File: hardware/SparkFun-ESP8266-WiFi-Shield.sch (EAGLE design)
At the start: 61 parts, among them Q1 BSS138, Q2 BSS138, U1 AP2112K-3.3V, U2 ESP8266, U3 AT25SF041-SOIC8, Y1 26MHz

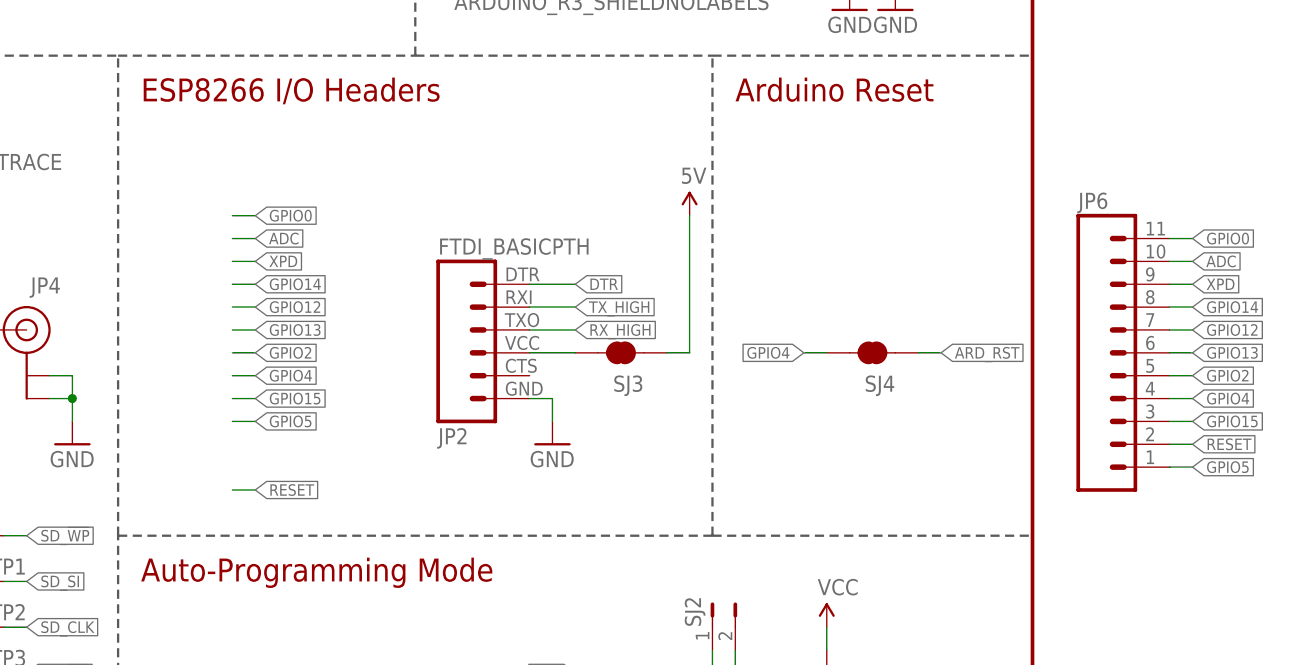
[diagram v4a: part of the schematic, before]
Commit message: Cleaning up schematic.
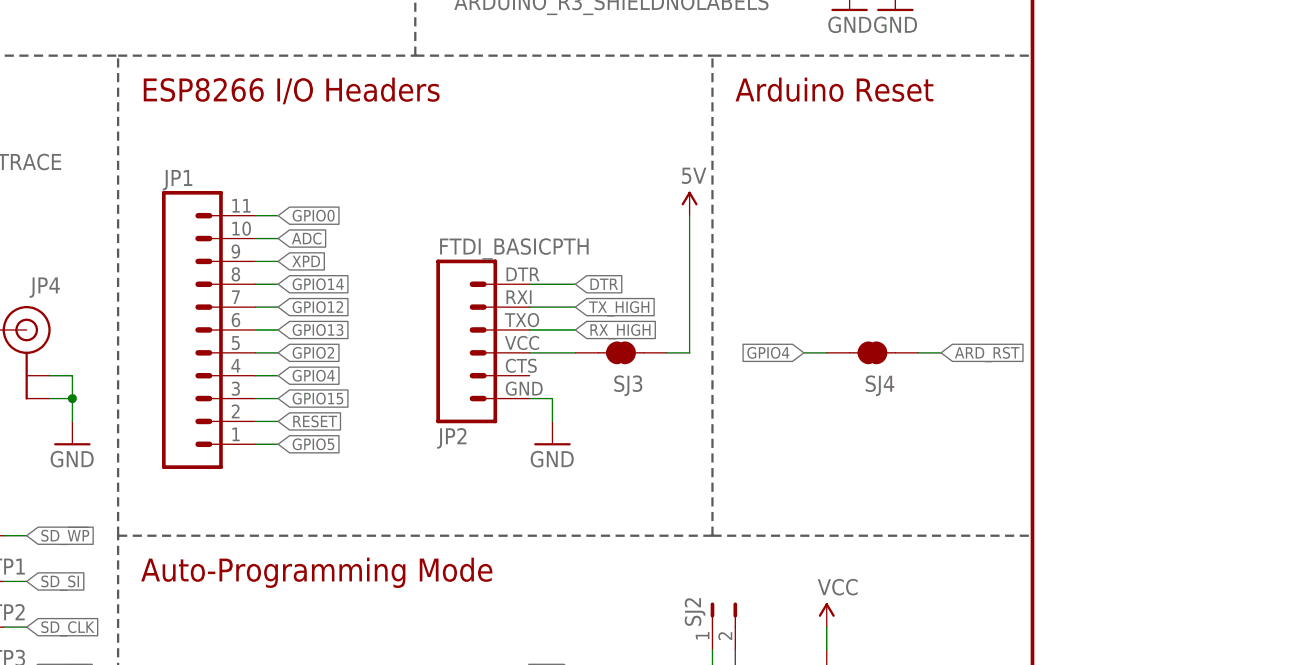
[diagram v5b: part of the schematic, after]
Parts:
- removed JP6: (no value), SparkFun-Connectors:M11PTH
- added JP1: (no value), SparkFun-Connectors:M11PTH
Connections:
- net ADC: now also JP1.10; no longer JP6.10
- net GPIO0: now also JP1.11; no longer JP6.11
- net GPIO12: now also JP1.7; no longer JP6.7
- net GPIO13: now also JP1.6; no longer JP6.6
- net GPIO14: now also JP1.8; no longer JP6.8
- net GPIO15: now also JP1.3; no longer JP6.3
- net GPIO2: now also JP1.5; no longer JP6.5
- net GPIO4: now also JP1.4; no longer JP6.4
- net GPIO5: now also JP1.1; no longer JP6.1
- net RESET: now also JP1.2; no longer JP6.2
- net XPD: now also JP1.9; no longer JP6.9
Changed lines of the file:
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@@
 <part name="SJ1" library="SparkFun-Passives" deviceset="JUMPER-PAD-2-NO" device="" value=""/>
 <part name="SJ2" library="SparkFun-Passives" deviceset="JUMPER-PTH-2-NO" device="" value=""/>
-<part name="JP6" library="SparkFun-Connectors" deviceset="M11" device="PTH"/>
+<part name="JP1" library="SparkFun-Connectors" deviceset="M11" device="PTH"/>
 </parts>
 <sheets>
@@
 <instance part="SJ1" gate="G$1" x="208.28" y="43.18"/>
 <instance part="SJ2" gate="G$1" x="213.36" y="58.42"/>
-<instance part="JP6" gate="G$1" x="254" y="88.9"/>
+<instance part="JP1" gate="G$1" x="152.4" y="91.44"/>
 </instances>
 <busses>
@@
 </segment>
 <segment>
-<wire x1="160.02" y1="73.66" x2="162.56" y2="73.66" width="0.1524" layer="91"/>
-<label x="162.56" y="73.66" size="1.27" layer="95" xref="yes"/>
-</segment>
-<segment>
-<pinref part="JP6" gate="G$1" pin="2"/>
-<wire x1="264.16" y1="78.74" x2="266.7" y2="78.74" width="0.1524" layer="91"/>
-<label x="266.7" y="78.74" size="1.27" layer="95" xref="yes"/>
+<pinref part="JP1" gate="G$1" pin="2"/>
+<wire x1="162.56" y1="81.28" x2="165.1" y2="81.28" width="0.1524" layer="91"/>
+<label x="165.1" y="81.28" size="1.27" layer="95" xref="yes"/>
 </segment>
 </net>
@@
 </segment>
 <segment>
-<wire x1="160.02" y1="96.52" x2="162.56" y2="96.52" width="0.1524" layer="91"/>
-<label x="162.56" y="96.52" size="1.27" layer="95" xref="yes"/>
-</segment>
-<segment>
-<pinref part="JP6" gate="G$1" pin="8"/>
-<wire x1="264.16" y1="93.98" x2="266.7" y2="93.98" width="0.1524" layer="91"/>
-<label x="266.7" y="93.98" size="1.27" layer="95" xref="yes"/>
+<pinref part="JP1" gate="G$1" pin="8"/>
+<wire x1="162.56" y1="96.52" x2="165.1" y2="96.52" width="0.1524" layer="91"/>
+<label x="165.1" y="96.52" size="1.27" layer="95" xref="yes"/>
 </segment>
 </net>
@@
 </segment>
 <segment>
-<wire x1="160.02" y1="101.6" x2="162.56" y2="101.6" width="0.1524" layer="91"/>
-<label x="162.56" y="101.6" size="1.27" layer="95" xref="yes"/>
-</segment>
-<segment>
-<pinref part="JP6" gate="G$1" pin="10"/>
-<wire x1="264.16" y1="99.06" x2="266.7" y2="99.06" width="0.1524" layer="91"/>
-<label x="266.7" y="99.06" size="1.27" layer="95" xref="yes"/>
+<pinref part="JP1" gate="G$1" pin="10"/>
+<wire x1="162.56" y1="101.6" x2="165.1" y2="101.6" width="0.1524" layer="91"/>
+<label x="165.1" y="101.6" size="1.27" layer="95" xref="yes"/>
 </segment>
 </net>
@@
 </segment>
 <segment>
-<wire x1="160.02" y1="104.14" x2="162.56" y2="104.14" width="0.1524" layer="91"/>
-<label x="162.56" y="104.14" size="1.27" layer="95" xref="yes"/>
-</segment>
-<segment>
-<pinref part="JP6" gate="G$1" pin="11"/>
-<wire x1="264.16" y1="101.6" x2="266.7" y2="101.6" width="0.1524" layer="91"/>
-<label x="266.7" y="101.6" size="1.27" layer="95" xref="yes"/>
+<pinref part="JP1" gate="G$1" pin="11"/>
+<wire x1="162.56" y1="104.14" x2="165.1" y2="104.14" width="0.1524" layer="91"/>
+<label x="165.1" y="104.14" size="1.27" layer="95" xref="yes"/>
 </segment>
 </net>
@@
 </segment>
 <segment>
-<wire x1="160.02" y1="81.28" x2="162.56" y2="81.28" width="0.1524" layer="91"/>
-<label x="162.56" y="81.28" size="1.27" layer="95" xref="yes"/>
-</segment>
-<segment>
-<pinref part="JP6" gate="G$1" pin="1"/>
-<wire x1="264.16" y1="76.2" x2="266.7" y2="76.2" width="0.1524" layer="91"/>
-<label x="266.7" y="76.2" size="1.27" layer="95" xref="yes"/>
+<pinref part="JP1" gate="G$1" pin="1"/>
+<wire x1="162.56" y1="78.74" x2="165.1" y2="78.74" width="0.1524" layer="91"/>
+<label x="165.1" y="78.74" size="1.27" layer="95" xref="yes"/>
 </segment>
 </net>
@@
 </segment>
 <segment>
-<wire x1="160.02" y1="86.36" x2="162.56" y2="86.36" width="0.1524" layer="91"/>
-<label x="162.56" y="86.36" size="1.27" layer="95" xref="yes"/>
-</segment>
-<segment>
 <pinref part="SJ4" gate="G$1" pin="2"/>
 <wire x1="226.06" y1="88.9" x2="223.52" y2="88.9" width="0.1524" layer="91"/>
@@
 </segment>
 <segment>
-<pinref part="JP6" gate="G$1" pin="4"/>
-<wire x1="264.16" y1="83.82" x2="266.7" y2="83.82" width="0.1524" layer="91"/>
-<label x="266.7" y="83.82" size="1.27" layer="95" xref="yes"/>
+<pinref part="JP1" gate="G$1" pin="4"/>
+<wire x1="162.56" y1="86.36" x2="165.1" y2="86.36" width="0.1524" layer="91"/>
+<label x="165.1" y="86.36" size="1.27" layer="95" xref="yes"/>
 </segment>
 </net>
@@
 </segment>
 <segment>
-<wire x1="160.02" y1="99.06" x2="162.56" y2="99.06" width="0.1524" layer="91"/>
-<label x="162.56" y="99.06" size="1.27" layer="95" xref="yes"/>
-</segment>
-<segment>
-<pinref part="JP6" gate="G$1" pin="9"/>
-<wire x1="264.16" y1="96.52" x2="266.7" y2="96.52" width="0.1524" layer="91"/>
-<label x="266.7" y="96.52" size="1.27" layer="95" xref="yes"/>
+<pinref part="JP1" gate="G$1" pin="9"/>
+<wire x1="162.56" y1="99.06" x2="165.1" y2="99.06" width="0.1524" layer="91"/>
+<label x="165.1" y="99.06" size="1.27" layer="95" xref="yes"/>
 </segment>
 </net>
@@
 </segment>
 <segment>
-<wire x1="160.02" y1="83.82" x2="162.56" y2="83.82" width="0.1524" layer="91"/>
-<label x="162.56" y="83.82" size="1.27" layer="95" xref="yes"/>
-</segment>
-<segment>
-<pinref part="JP6" gate="G$1" pin="3"/>
-<wire x1="264.16" y1="81.28" x2="266.7" y2="81.28" width="0.1524" layer="91"/>
-<label x="266.7" y="81.28" size="1.27" layer="95" xref="yes"/>
+<pinref part="JP1" gate="G$1" pin="3"/>
+<wire x1="162.56" y1="83.82" x2="165.1" y2="83.82" width="0.1524" layer="91"/>
+<label x="165.1" y="83.82" size="1.27" layer="95" xref="yes"/>
 </segment>
 </net>
@@
 </segment>
 <segment>
-<wire x1="160.02" y1="91.44" x2="162.56" y2="91.44" width="0.1524" layer="91"/>
-<label x="162.56" y="91.44" size="1.27" layer="95" xref="yes"/>
-</segment>
-<segment>
-<pinref part="JP6" gate="G$1" pin="6"/>
-<wire x1="264.16" y1="88.9" x2="266.7" y2="88.9" width="0.1524" layer="91"/>
-<label x="266.7" y="88.9" size="1.27" layer="95" xref="yes"/>
+<pinref part="JP1" gate="G$1" pin="6"/>
+<wire x1="162.56" y1="91.44" x2="165.1" y2="91.44" width="0.1524" layer="91"/>
+<label x="165.1" y="91.44" size="1.27" layer="95" xref="yes"/>
 </segment>
 </net>
@@
 </segment>
 <segment>
-<wire x1="160.02" y1="93.98" x2="162.56" y2="93.98" width="0.1524" layer="91"/>
-<label x="162.56" y="93.98" size="1.27" layer="95" xref="yes"/>
-</segment>
-<segment>
-<pinref part="JP6" gate="G$1" pin="7"/>
-<wire x1="264.16" y1="91.44" x2="266.7" y2="91.44" width="0.1524" layer="91"/>
-<label x="266.7" y="91.44" size="1.27" layer="95" xref="yes"/>
+<pinref part="JP1" gate="G$1" pin="7"/>
+<wire x1="162.56" y1="93.98" x2="165.1" y2="93.98" width="0.1524" layer="91"/>
+<label x="165.1" y="93.98" size="1.27" layer="95" xref="yes"/>
 </segment>
 </net>
@@
 </segment>
 <segment>
-<wire x1="160.02" y1="88.9" x2="162.56" y2="88.9" width="0.1524" layer="91"/>
-<label x="162.56" y="88.9" size="1.27" layer="95" xref="yes"/>
-</segment>
-<segment>
-<pinref part="JP6" gate="G$1" pin="5"/>
-<wire x1="264.16" y1="86.36" x2="266.7" y2="86.36" width="0.1524" layer="91"/>
-<label x="266.7" y="86.36" size="1.27" layer="95" xref="yes"/>
-</segment>
-</net>
+<pinref part="JP1" gate="G$1" pin="5"/>
+<wire x1="162.56" y1="88.9" x2="165.1" y2="88.9" width="0.1524" layer="91"/>
+<label x="165.1" y="88.9" size="1.27" layer="95" xref="yes"/>
+</segment>
+</net>

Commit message: Minor mods after running checklist.
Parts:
- SJ4: value JUMPER-PAD-2-NC_BY_TRACE -> JUMPER-PAD-2-NOYES_SILK; device SparkFun-Passives:JUMPER-PAD-2-NC_BY_TRACE -> SparkFun-Passives:JUMPER-PAD-2-NOYES_SILK
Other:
- note added: "SJ3 allows powering the ESP8266 from an FTDI cable. (Default: closed)."
- note added: "SJ4 connects the ESP8266 GPIO4 pin to the Arduino reset pin. With the proper ESP8266 firmware, this enables wireless Arduino bootloading. (Default: open)"
- moved on the sheet: JP2, SJ3
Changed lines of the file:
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@@
 <drawing>
 <settings>
-<setting alwaysvectorfont="no"/>
+<setting alwaysvectorfont="yes"/>
 <setting verticaltext="up"/>
 </settings>
@@
 <part name="JP4" library="SparkFun-Connectors" deviceset="U.FL" device="" value="U.FL"/>
 <part name="SUPPLY15" library="SparkFun-Aesthetics" deviceset="VCC" device=""/>
-<part name="SJ4" library="SparkFun-Passives" deviceset="JUMPER-PAD-2-NC_BY_TRACE" device="" value=""/>
 <part name="SJ1" library="SparkFun-Passives" deviceset="JUMPER-PAD-2-NO" device="" value=""/>
 <part name="SJ2" library="SparkFun-Passives" deviceset="JUMPER-PTH-2-NO" device="" value=""/>
 <part name="JP1" library="SparkFun-Connectors" deviceset="M11" device="PTH"/>
+<part name="SJ4" library="SparkFun-Passives" deviceset="JUMPER-PAD-2-NO" device="YES_SILK" value=""/>
 </parts>
 <sheets>
@@
 <wire x1="213.36" y1="68.58" x2="213.36" y2="121.92" width="0.254" layer="97" style="longdash"/>
 <text x="215.9" y="116.84" size="2.54" layer="94">Arduino Reset</text>
+<text x="215.9" y="96.52" size="1.27" layer="97">SJ4 connects the ESP8266
+GPIO4 pin to the Arduino
+reset pin. With the proper
+ESP8266 firmware, this
+enables wireless Arduino
+bootloading.
+(Default: open)</text>
+<text x="190.5" y="76.2" size="1.27" layer="97">SJ3 allows powering
+the ESP8266 from
+an FTDI cable.
+(Default: closed).</text>
 </plain>
 <instances>
@@
 <instance part="SUPPLY11" gate="G$1" x="157.48" y="172.72"/>
 <instance part="SUPPLY7" gate="G$1" x="116.84" y="175.26"/>
-<instance part="JP2" gate="G$1" x="187.96" y="91.44" rot="MR180"/>
-<instance part="GND17" gate="1" x="195.58" y="78.74"/>
-<instance part="SUPPLY12" gate="G$1" x="210.82" y="104.14"/>
+<instance part="JP2" gate="G$1" x="180.34" y="91.44" rot="MR180"/>
+<instance part="GND17" gate="1" x="187.96" y="78.74"/>
+<instance part="SUPPLY12" gate="G$1" x="203.2" y="104.14"/>
 <instance part="LOGO1" gate="G$1" x="0" y="0"/>
 <instance part="STANDOFF1" gate="G$1" x="243.84" y="33.02"/>
@@
 <instance part="S1" gate="G$1" x="127" y="137.16"/>
 <instance part="D2" gate="G$1" x="99.06" y="53.34" rot="R270"/>
-<instance part="SJ3" gate="G$1" x="203.2" y="88.9" rot="R180"/>
+<instance part="SJ3" gate="G$1" x="195.58" y="88.9" rot="R180"/>
 <instance part="JP4" gate="G$1" x="137.16" y="91.44" rot="MR0"/>
 <instance part="SUPPLY15" gate="G$1" x="104.14" y="55.88"/>
-<instance part="SJ4" gate="G$1" x="231.14" y="88.9" rot="R180"/>
 <instance part="SJ1" gate="G$1" x="208.28" y="43.18"/>
 <instance part="SJ2" gate="G$1" x="213.36" y="58.42"/>
 <instance part="JP1" gate="G$1" x="152.4" y="91.44"/>
+<instance part="SJ4" gate="G$1" x="231.14" y="88.9" rot="R180"/>
 </instances>
 <busses>
@@
 <segment>
 <pinref part="JP2" gate="G$1" pin="6"/>
-<wire x1="193.04" y1="83.82" x2="195.58" y2="83.82" width="0.1524" layer="91"/>
-<wire x1="195.58" y1="83.82" x2="195.58" y2="81.28" width="0.1524" layer="91"/>
+<wire x1="185.42" y1="83.82" x2="187.96" y2="83.82" width="0.1524" layer="91"/>
+<wire x1="187.96" y1="83.82" x2="187.96" y2="81.28" width="0.1524" layer="91"/>
 <pinref part="GND17" gate="1" pin="GND"/>
 </segment>
@@
 <segment>
 <pinref part="JP2" gate="G$1" pin="1"/>
-<wire x1="193.04" y1="96.52" x2="198.12" y2="96.52" width="0.1524" layer="91"/>
-<label x="198.12" y="96.52" size="1.27" layer="95" xref="yes"/>
+<wire x1="185.42" y1="96.52" x2="190.5" y2="96.52" width="0.1524" layer="91"/>
+<label x="190.5" y="96.52" size="1.27" layer="95" xref="yes"/>
 </segment>
 </net>
@@
 </segment>
 <segment>
-<pinref part="SJ4" gate="G$1" pin="2"/>
 <wire x1="226.06" y1="88.9" x2="223.52" y2="88.9" width="0.1524" layer="91"/>
 <label x="223.52" y="88.9" size="1.27" layer="95" rot="R180" xref="yes"/>
+<pinref part="SJ4" gate="G$1" pin="2"/>
 </segment>
 <segment>
@@
 <segment>
 <pinref part="JP2" gate="G$1" pin="2"/>
-<wire x1="193.04" y1="93.98" x2="198.12" y2="93.98" width="0.1524" layer="91"/>
-<label x="198.12" y="93.98" size="1.27" layer="95" xref="yes"/>
+<wire x1="185.42" y1="93.98" x2="190.5" y2="93.98" width="0.1524" layer="91"/>
+<label x="190.5" y="93.98" size="1.27" layer="95" xref="yes"/>
 </segment>
 <segment>
@@
 <segment>
 <pinref part="SUPPLY12" gate="G$1" pin="5V"/>
-<wire x1="208.28" y1="88.9" x2="210.82" y2="88.9" width="0.1524" layer="91"/>
-<wire x1="210.82" y1="88.9" x2="210.82" y2="104.14" width="0.1524" layer="91"/>
+<wire x1="200.66" y1="88.9" x2="203.2" y2="88.9" width="0.1524" layer="91"/>
+<wire x1="203.2" y1="88.9" x2="203.2" y2="104.14" width="0.1524" layer="91"/>
 <pinref part="SJ3" gate="G$1" pin="1"/>
 </segment>
@@
 <segment>
 <pinref part="JP2" gate="G$1" pin="3"/>
-<wire x1="193.04" y1="91.44" x2="198.12" y2="91.44" width="0.1524" layer="91"/>
-<label x="198.12" y="91.44" size="1.27" layer="95" xref="yes"/>
+<wire x1="185.42" y1="91.44" x2="190.5" y2="91.44" width="0.1524" layer="91"/>
+<label x="190.5" y="91.44" size="1.27" layer="95" xref="yes"/>
 </segment>
 <segment>
@@
 </segment>
 <segment>
-<pinref part="SJ4" gate="G$1" pin="1"/>
 <wire x1="236.22" y1="88.9" x2="238.76" y2="88.9" width="0.1524" layer="91"/>
 <label x="238.76" y="88.9" size="1.27" layer="95" xref="yes"/>
+<pinref part="SJ4" gate="G$1" pin="1"/>
 </segment>
 </net>
@@
 <segment>
 <pinref part="JP2" gate="G$1" pin="4"/>
-<wire x1="193.04" y1="88.9" x2="198.12" y2="88.9" width="0.1524" layer="91"/>
+<wire x1="185.42" y1="88.9" x2="190.5" y2="88.9" width="0.1524" layer="91"/>
 <pinref part="SJ3" gate="G$1" pin="2"/>
 </segment>
